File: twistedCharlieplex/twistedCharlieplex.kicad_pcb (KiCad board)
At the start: 2 copper layers, 54.9 x 54.9 mm, 69 parts

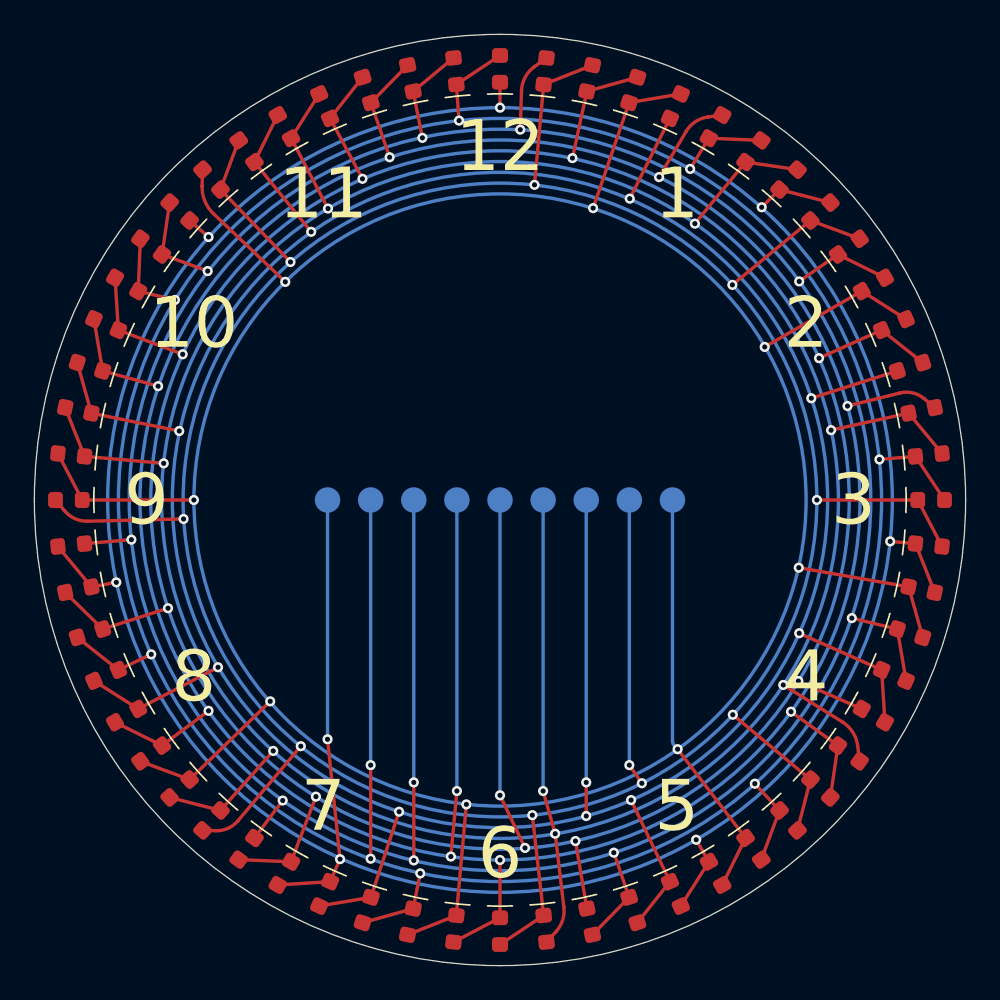
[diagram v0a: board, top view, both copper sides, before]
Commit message: Component layout locked. Trace nightmare time.
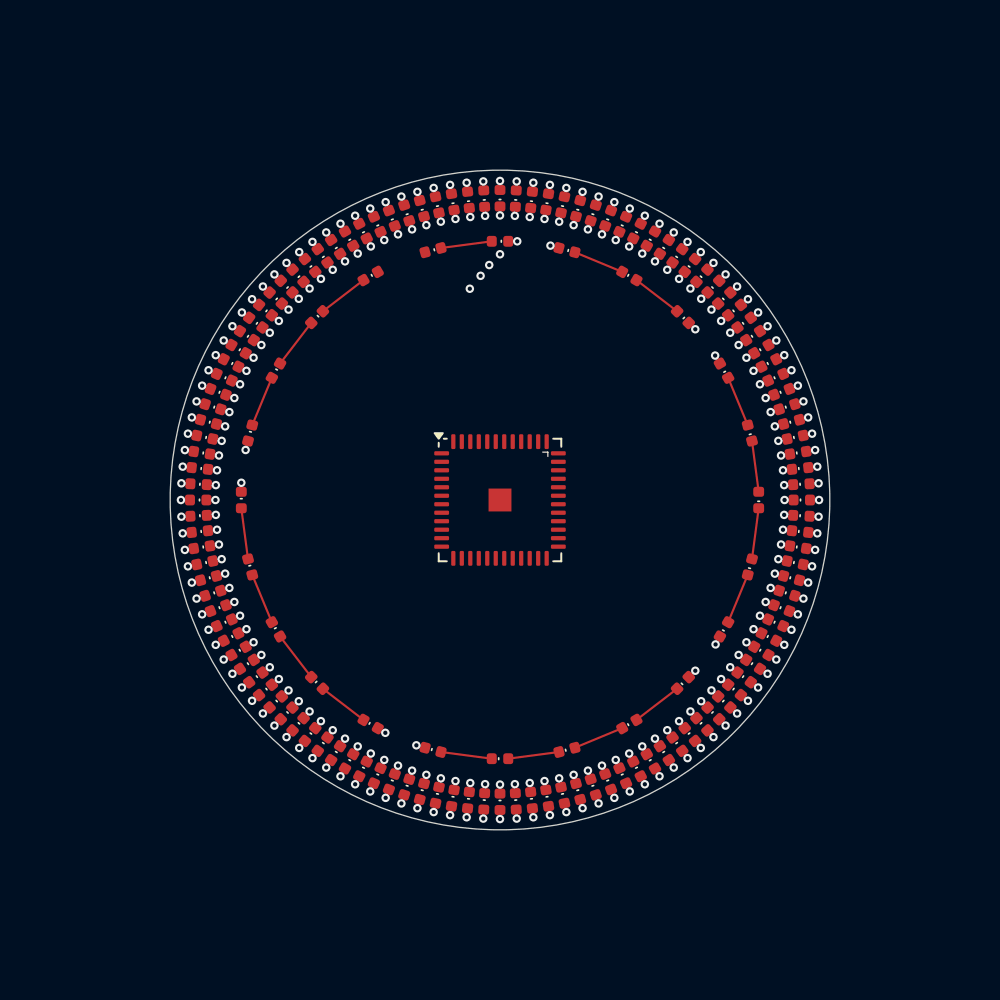
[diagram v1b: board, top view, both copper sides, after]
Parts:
- removed IO0, IO1, IO2, IO3, IO4, IO5, IO6, IO7, IO8: TestPoint, TestPoint:TestPoint_Pad_D1.5mm
- added D100: LED_Small, LED_SMD:LED_0402_1005Metric, F.Cu at (14.9, 9.68)
- added D101: LED_Small, LED_SMD:LED_0402_1005Metric, F.Cu at (15.8, 8.07)
- added D102: LED_Small, LED_SMD:LED_0402_1005Metric, F.Cu at (16.6, 6.37)
- added D103: LED_Small, LED_SMD:LED_0402_1005Metric, F.Cu at (17.2, 4.60)
- added D104: LED_Small, LED_SMD:LED_0402_1005Metric, F.Cu at (17.6, 2.78)
- added D105: LED_Small, LED_SMD:LED_0402_1005Metric, F.Cu at (17.8, 0.93)
- added D106: LED_Small, LED_SMD:LED_0402_1005Metric, F.Cu at (17.8, -0.93)
- added D107: LED_Small, LED_SMD:LED_0402_1005Metric, F.Cu at (17.6, -2.78)
- added D108: LED_Small, LED_SMD:LED_0402_1005Metric, F.Cu at (17.2, -4.60)
- added D109: LED_Small, LED_SMD:LED_0402_1005Metric, F.Cu at (16.6, -6.37)
- added D110: LED_Small, LED_SMD:LED_0402_1005Metric, F.Cu at (15.8, -8.07)
- added D111: LED_Small, LED_SMD:LED_0402_1005Metric, F.Cu at (14.9, -9.68)
- added D112: LED_Small, LED_SMD:LED_0402_1005Metric, F.Cu at (13.8, -11.2)
- added D113: LED_Small, LED_SMD:LED_0402_1005Metric, F.Cu at (12.6, -12.6)
- added D114: LED_Small, LED_SMD:LED_0402_1005Metric, F.Cu at (11.2, -13.8)
- added D115: LED_Small, LED_SMD:LED_0402_1005Metric, F.Cu at (9.68, -14.9)
- added D116: LED_Small, LED_SMD:LED_0402_1005Metric, F.Cu at (8.07, -15.8)
- added D117: LED_Small, LED_SMD:LED_0402_1005Metric, F.Cu at (6.37, -16.6)
- added D118: LED_Small, LED_SMD:LED_0402_1005Metric, F.Cu at (4.60, -17.2)
- added D119: LED_Small, LED_SMD:LED_0402_1005Metric, F.Cu at (2.78, -17.6)
- added D120: LED_Small, LED_SMD:LED_0402_1005Metric, F.Cu at (0.93, -17.8)
- added D121: LED_Small, LED_SMD:LED_0402_1005Metric, F.Cu at (-3.94, -14.7)
- added D122: LED_Small, LED_SMD:LED_0402_1005Metric, F.Cu at (-7.62, -13.2)
- added D123: LED_Small, LED_SMD:LED_0402_1005Metric, F.Cu at (-10.8, -10.8)
- added D124: LED_Small, LED_SMD:LED_0402_1005Metric, F.Cu at (-13.2, -7.62)
- added D125: LED_Small, LED_SMD:LED_0402_1005Metric, F.Cu at (-14.7, -3.94)
- added D126: LED_Small, LED_SMD:LED_0402_1005Metric, F.Cu at (-15.2, 0.00)
- added D127: LED_Small, LED_SMD:LED_0402_1005Metric, F.Cu at (-14.7, 3.94)
- added D128: LED_Small, LED_SMD:LED_0402_1005Metric, F.Cu at (-13.2, 7.62)
- added D129: LED_Small, LED_SMD:LED_0402_1005Metric, F.Cu at (-10.8, 10.8)
- added D130: LED_Small, LED_SMD:LED_0402_1005Metric, F.Cu at (-7.62, 13.2)
- added D131: LED_Small, LED_SMD:LED_0402_1005Metric, F.Cu at (-3.94, 14.7)
- added D132: LED_Small, LED_SMD:LED_0402_1005Metric, F.Cu at (0.00, 15.2)
- added D133: LED_Small, LED_SMD:LED_0402_1005Metric, F.Cu at (3.94, 14.7)
- added D134: LED_Small, LED_SMD:LED_0402_1005Metric, F.Cu at (7.62, 13.2)
- added D135: LED_Small, LED_SMD:LED_0402_1005Metric, F.Cu at (10.8, 10.8)
- added D136: LED_Small, LED_SMD:LED_0402_1005Metric, F.Cu at (13.2, 7.62)
- added D137: LED_Small, LED_SMD:LED_0402_1005Metric, F.Cu at (14.7, 3.94)
- added D138: LED_Small, LED_SMD:LED_0402_1005Metric, F.Cu at (15.2, 0.00)
- added D139: LED_Small, LED_SMD:LED_0402_1005Metric, F.Cu at (14.7, -3.94)
- added D140: LED_Small, LED_SMD:LED_0402_1005Metric, F.Cu at (13.2, -7.62)
- added D141: LED_Small, LED_SMD:LED_0402_1005Metric, F.Cu at (10.8, -10.8)
- added D142: LED_Small, LED_SMD:LED_0402_1005Metric, F.Cu at (7.62, -13.2)
- added D143: LED_Small, LED_SMD:LED_0402_1005Metric, F.Cu at (3.94, -14.7)
- added D144: LED_Small, LED_SMD:LED_0402_1005Metric, F.Cu at (0.00, -15.2)
- added D61: LED_Small, LED_SMD:LED_0402_1005Metric, F.Cu at (-0.93, -17.8)
- added D62: LED_Small, LED_SMD:LED_0402_1005Metric, F.Cu at (-2.78, -17.6)
- added D63: LED_Small, LED_SMD:LED_0402_1005Metric, F.Cu at (-4.60, -17.2)
- added D64: LED_Small, LED_SMD:LED_0402_1005Metric, F.Cu at (-6.37, -16.6)
- added D65: LED_Small, LED_SMD:LED_0402_1005Metric, F.Cu at (-8.07, -15.8)
- added D66: LED_Small, LED_SMD:LED_0402_1005Metric, F.Cu at (-9.68, -14.9)
- added D67: LED_Small, LED_SMD:LED_0402_1005Metric, F.Cu at (-11.2, -13.8)
- added D68: LED_Small, LED_SMD:LED_0402_1005Metric, F.Cu at (-12.6, -12.6)
- added D69: LED_Small, LED_SMD:LED_0402_1005Metric, F.Cu at (-13.8, -11.2)
- added D70: LED_Small, LED_SMD:LED_0402_1005Metric, F.Cu at (-14.9, -9.68)
- added D71: LED_Small, LED_SMD:LED_0402_1005Metric, F.Cu at (-15.8, -8.07)
- added D72: LED_Small, LED_SMD:LED_0402_1005Metric, F.Cu at (-16.6, -6.37)
- added D73: LED_Small, LED_SMD:LED_0402_1005Metric, F.Cu at (-17.2, -4.60)
- added D74: LED_Small, LED_SMD:LED_0402_1005Metric, F.Cu at (-17.6, -2.78)
- added D75: LED_Small, LED_SMD:LED_0402_1005Metric, F.Cu at (-17.8, -0.93)
- added D76: LED_Small, LED_SMD:LED_0402_1005Metric, F.Cu at (-17.8, 0.93)
- added D77: LED_Small, LED_SMD:LED_0402_1005Metric, F.Cu at (-17.6, 2.78)
- added D78: LED_Small, LED_SMD:LED_0402_1005Metric, F.Cu at (-17.2, 4.60)
- added D79: LED_Small, LED_SMD:LED_0402_1005Metric, F.Cu at (-16.6, 6.37)
- added D80: LED_Small, LED_SMD:LED_0402_1005Metric, F.Cu at (-15.8, 8.07)
- added D81: LED_Small, LED_SMD:LED_0402_1005Metric, F.Cu at (-14.9, 9.68)
- added D82: LED_Small, LED_SMD:LED_0402_1005Metric, F.Cu at (-13.8, 11.2)
- added D83: LED_Small, LED_SMD:LED_0402_1005Metric, F.Cu at (-12.6, 12.6)
- added D84: LED_Small, LED_SMD:LED_0402_1005Metric, F.Cu at (-11.2, 13.8)
- added D85: LED_Small, LED_SMD:LED_0402_1005Metric, F.Cu at (-9.68, 14.9)
- added D86: LED_Small, LED_SMD:LED_0402_1005Metric, F.Cu at (-8.07, 15.8)
- added D87: LED_Small, LED_SMD:LED_0402_1005Metric, F.Cu at (-6.37, 16.6)
- added D88: LED_Small, LED_SMD:LED_0402_1005Metric, F.Cu at (-4.60, 17.2)
- added D89: LED_Small, LED_SMD:LED_0402_1005Metric, F.Cu at (-2.78, 17.6)
- added D90: LED_Small, LED_SMD:LED_0402_1005Metric, F.Cu at (-0.93, 17.8)
- added D91: LED_Small, LED_SMD:LED_0402_1005Metric, F.Cu at (0.93, 17.8)
- added D92: LED_Small, LED_SMD:LED_0402_1005Metric, F.Cu at (2.78, 17.6)
- added D93: LED_Small, LED_SMD:LED_0402_1005Metric, F.Cu at (4.60, 17.2)
- added D94: LED_Small, LED_SMD:LED_0402_1005Metric, F.Cu at (6.37, 16.6)
- added D95: LED_Small, LED_SMD:LED_0402_1005Metric, F.Cu at (8.07, 15.8)
- added D96: LED_Small, LED_SMD:LED_0402_1005Metric, F.Cu at (9.68, 14.9)
- added D97: LED_Small, LED_SMD:LED_0402_1005Metric, F.Cu at (11.2, 13.8)
- added D98: LED_Small, LED_SMD:LED_0402_1005Metric, F.Cu at (12.6, 12.6)
- added D99: LED_Small, LED_SMD:LED_0402_1005Metric, F.Cu at (13.8, 11.2)
- added U2: STM32L412CBUxP, Package_DFN_QFN:QFN-48-1EP_7x7mm_P0.5mm_EP5.6x5.6mm, F.Cu at (0.00, 0.00)
- D1, D10, D11, D12, D13, D14, D15, D16, D17, D18, D19, D2, D20, D21, D22, D23, D24, D25, D26, D27, D28, D29, D3, D30, D31, D32, D33, D34, D35, D36, D37, D38, D39, D4, D40, D41, D42, D43, D44, D45, D46, D47, D48, D49, D5, D50, D51, D52, D53, D54, D55, D56, D57, D58, D59, D6, D60, D7, D8, D9: footprint LED_SMD:LED_0603_1608Metric -> LED_SMD:LED_0402_1005Metric
- moved D13 7.62 mm to (-16.9, -5.49)
- moved D19 7.62 mm to (-16.9, 5.49)
- moved D28 7.62 mm to (-5.49, 16.9)
- moved D34 7.62 mm to (5.49, 16.9)
- moved D4 7.62 mm to (-5.49, -16.9)
- moved D43 7.62 mm to (16.9, 5.49)
- moved D49 7.62 mm to (16.9, -5.49)
- moved D58 7.62 mm to (5.49, -16.9)
- moved D12 7.62 mm to (-16.2, -7.23)
- moved D20 7.62 mm to (-16.2, 7.23)
- moved D27 7.62 mm to (-7.23, 16.2)
- moved D35 7.62 mm to (7.23, 16.2)
- moved D42 7.62 mm to (16.2, 7.23)
- moved D5 7.62 mm to (-7.23, -16.2)
- moved D50 7.62 mm to (16.2, -7.23)
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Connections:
- net /IO0 renamed /Charlie Displays/IO0
- net /IO1 renamed /Charlie Displays/IO1
- net /IO2 renamed /Charlie Displays/IO2
- net /IO3 renamed /Charlie Displays/IO3
- net /IO4 renamed /Charlie Displays/IO4
- net /IO5 renamed /Charlie Displays/IO5
- net /IO6 renamed /Charlie Displays/IO6
- net /IO7 renamed /Charlie Displays/IO7
- net /IO8 renamed /Charlie Displays/IO8
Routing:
- net /Charlie Displays/IO8: track 91.1 -> 27.2 mm, vias 8 -> 15
- net /Charlie Displays/IO7: track 87.1 -> 24.0 mm, vias 10 -> 14
- net /Charlie Displays/IO6: track 79.6 -> 24.0 mm, vias 10 -> 14
- net /Charlie Displays/IO5: track 72.1 -> 20.1 mm, vias 8 -> 12
- net /Charlie Displays/IO4: track 71.8 -> 24.0 mm, vias 10 -> 14
- net /Charlie Displays/IO3: track 64.6 -> 20.1 mm, vias 9 -> 12
- net /Charlie Displays/IO2: track 61.0 -> 20.7 mm, vias 10 -> 13
- net /Charlie Displays/IO11: track 0.00 -> 30.9 mm, vias 0 -> 15
- net /Charlie Displays/IO1: track 57.8 -> 30.2 mm, vias 9 -> 15
- net /Charlie Displays/IO18: track 0.00 -> 27.2 mm, vias 0 -> 15
- net /Charlie Displays/IO16: track 0.00 -> 24.0 mm, vias 0 -> 14
- net /Charlie Displays/IO17: track 0.00 -> 24.0 mm, vias 0 -> 14
- net /Charlie Displays/IO14: track 0.00 -> 24.0 mm, vias 0 -> 14
- net /Charlie Displays/IO10: track 0.00 -> 23.0 mm, vias 0 -> 13
- net /Charlie Displays/IO12: track 0.00 -> 20.7 mm, vias 0 -> 13
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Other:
- board size 54.9 x 54.9 mm -> 38.9 x 38.9 mm
- copper layers 2 -> 6
- board text removed: "1"
- board text removed: "10"
- board text removed: "11"
- board text removed: "12"
- board text removed: "2"
- board text removed: "3"
- board text removed: "4"
- board text removed: "5"
- board text removed: "6"
- board text removed: "7"
- board text removed: "8"
- board text removed: "9"

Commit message: Start of a layout. This is awful. I'm not sure I can make this happen in 4 layers. I may come back to this.
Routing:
- net /Charlie Displays/IO2: track 20.7 -> 48.9 mm, vias 13 -> 16
- net /Charlie Displays/IO12: track 20.7 -> 47.2 mm, vias 13 -> 16
- net /Charlie Displays/IO8: track 27.2 -> 49.1 mm, vias 15 -> 18
- net /Charlie Displays/IO1: track 30.2 -> 51.5 mm, vias 15 -> 16
- net /Charlie Displays/IO11: track 30.9 -> 48.0 mm, vias 15 -> 16
- net /Charlie Displays/IO18: track 27.2 -> 44.1 mm, vias 15 -> 18
- net /Charlie Displays/IO7: track 24.0 -> 38.4 mm, vias 14 -> 16
- net /Charlie Displays/IO6: track 24.0 -> 37.6 mm, vias 14 -> 15
- net /Charlie Displays/IO16: track 24.0 -> 36.6 mm, vias 14 -> 15
- net /Charlie Displays/IO17: track 24.0 -> 36.2 mm, vias 14 -> 16
- net /Charlie Displays/IO4: track 24.0 -> 33.8 mm, vias 14 -> 15
- net /Charlie Displays/IO13: track 20.1 -> 29.8 mm, vias 12 -> 13
- net /Charlie Displays/IO15: track 20.1 -> 29.6 mm, vias 12 -> 14
- net /Charlie Displays/IO14: track 24.0 -> 33.0 mm, vias 14 -> 15
- net /Charlie Displays/IO5: track 20.1 -> 28.5 mm, vias 12 -> 14
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
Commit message: spirograph layout. let the nightmares begin
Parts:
- added AE1: Antenna_Shield, Antenna_SMD:C209892, F.Cu at (8.99, -3.30)
- added C1: 100n, Capacitor_SMD:C_0402_1005Metric, F.Cu at (-1.75, -7.47)
- added C2: 10u, Capacitor_SMD:C_0402_1005Metric, F.Cu at (-2.69, -7.47)
- added C3: 100n, Capacitor_SMD:C_0402_1005Metric, F.Cu at (-4.62, 0.51)
- added C4: 4p3, Capacitor_SMD:C_0402_1005Metric, F.Cu at (-7.90, -2.44)
- added C5: 4p3, Capacitor_SMD:C_0402_1005Metric, F.Cu at (-7.90, -0.61)
- added C6: 12p, Capacitor_SMD:C_0402_1005Metric, F.Cu at (11.2, 1.17)
- added C7: 12p, Capacitor_SMD:C_0402_1005Metric, F.Cu at (11.2, -1.93)
- added Q1: Q_PMOS_GSD, Package_TO_SOT_SMD:SOT-523, F.Cu at (25.7, -4.34)
- added R1: 10k, Resistor_SMD:R_0402_1005Metric, F.Cu at (-1.50, -4.62)
- added R2: 10k, Resistor_SMD:R_0402_1005Metric, F.Cu at (0.79, -4.65)
- added R3: 10k, Resistor_SMD:R_0402_1005Metric, F.Cu at (0.25, -5.61)
- added R4: 100k, Resistor_SMD:R_0402_1005Metric, F.Cu at (5.49, -3.58)
- added R5: 1M, Resistor_SMD:R_0402_1005Metric, F.Cu at (24.1, -4.34)
- added U1: STM32L412CBUx, Package_DFN_QFN:QFN-48-1EP_7x7mm_P0.5mm_EP5.6x5.6mm, F.Cu at (0.00, 0.00)
- added U3: ESP32-C3, Package_DFN_QFN:QFN-32-1EP_5x5mm_P0.5mm_EP3.7x3.7mm, F.Cu at (7.24, 0.00)
- added Y1: 32.768k, Crystal:Crystal_SMD_3215-2Pin_3.2x1.5mm, F.Cu at (-6.27, -1.52)
- added Y2: 40M, SMD_Crystal:Crystal_SMD_1612_4P, F.Cu at (11.2, -0.25)
- U2: value STM32L412CBUxP -> LIS2DW12; footprint Package_DFN_QFN:QFN-48-1EP_7x7mm_P0.5mm_EP5.6x5.6mm -> Package_LGA:LGA-12_2x2mm_P0.5mm
- moved U2 7.47 mm to (0.00, -7.47), turned to 180 degrees
- moved D122 4.19 mm to (-4.17, -15.6), turned to -165 degrees
- moved D128 4.19 mm to (-15.6, 4.17), turned to -75 degrees
- moved D134 4.19 mm to (4.17, 15.6), turned to 15 degrees
- moved D140 4.19 mm to (15.6, -4.17), turned to 105 degrees
- moved D121 4.19 mm to (0.00, -16.1), turned to 180 degrees
- moved D127 4.19 mm to (-16.1, 0.00), turned to -90 degrees
- moved D133 4.19 mm to (0.00, 16.1), turned to 0 degrees
- moved D139 4.19 mm to (16.1, 0.00), turned to 90 degrees
- moved D123 4.19 mm to (-8.06, -14.0), turned to -150 degrees
- moved D129 4.19 mm to (-14.0, 8.06), turned to -60 degrees
- moved D135 4.19 mm to (8.06, 14.0), turned to 30 degrees
- moved D141 4.19 mm to (14.0, -8.06), turned to 120 degrees
- moved D125 4.19 mm to (-14.0, -8.06), turned to -120 degrees
- moved D131 4.19 mm to (-8.06, 14.0), turned to -30 degrees
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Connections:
- net /Charlie Displays/IO0 renamed IO0
- net /Charlie Displays/IO1 renamed IO1
- net /Charlie Displays/IO10 renamed IO10
- net /Charlie Displays/IO11 renamed IO11
- net /Charlie Displays/IO12 renamed IO12
- net /Charlie Displays/IO13 renamed IO13
- net /Charlie Displays/IO14 renamed IO14
- net /Charlie Displays/IO15 renamed IO15
- net /Charlie Displays/IO16 renamed IO16
- net /Charlie Displays/IO17 renamed IO17
- net /Charlie Displays/IO18 renamed IO18
- net /Charlie Displays/IO2 renamed IO2
- net /Charlie Displays/IO20 renamed IO20
- net /Charlie Displays/IO21 renamed IO21
- net /Charlie Displays/IO22 renamed IO22
- net /Charlie Displays/IO23 renamed IO23
- net /Charlie Displays/IO24 renamed IO24
- net /Charlie Displays/IO25 renamed IO25
- net /Charlie Displays/IO3 renamed IO3
- net /Charlie Displays/IO4 renamed IO4
- net /Charlie Displays/IO5 renamed IO5
- net /Charlie Displays/IO6 renamed IO6
- net /Charlie Displays/IO7 renamed IO7
- net /Charlie Displays/IO8 renamed IO8
- U2 pad 1: VCC -> SCL
- U2 pad 10: unconnected-(U2-PA0-Pad10) -> +3V0
- U2 pad 12: unconnected-(U2-PA2-Pad12) -> WKUP1
- U2 pad 4: unconnected-(U2-PC15-Pad4) -> SDA
- U2 pad 6: unconnected-(U2-PH1-Pad6) -> GND
- U2 pad 7: unconnected-(U2-NRST-Pad7) -> GND
- U2 pad 9: VCC -> +3V0
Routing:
- net IO14: track 33.0 -> 146.0 mm, vias 15 -> 17
- net IO6: track 37.6 -> 146.9 mm, vias 15 -> 16
- net IO3: track 23.7 -> 130.1 mm, vias 12 -> 13
- net IO15: track 29.6 -> 131.3 mm, vias 14 -> 13
- net IO4: track 33.8 -> 135.5 mm, vias 15 -> 16
- net IO5: track 28.5 -> 129.0 mm, vias 14 -> 13
- net IO10: track 20.7 -> 121.0 mm, vias 13 -> 14
- net IO0: track 38.8 -> 138.2 mm, vias 15 -> 14
- net IO13: track 29.8 -> 119.7 mm, vias 13 -> 12
- net IO16: track 36.6 -> 126.3 mm, vias 15 -> 16
- net IO17: track 36.2 -> 122.9 mm, vias 16 -> 15
- net IO7: track 38.4 -> 124.7 mm, vias 16 -> 14
- net IO1: track 51.5 -> 136.4 mm, vias 16 -> 14
- net IO2: track 48.9 -> 130.0 mm, vias 16 -> 15
- net IO18: track 44.1 -> 123.9 mm, vias 18 -> 15
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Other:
- copper layers 6 -> 4

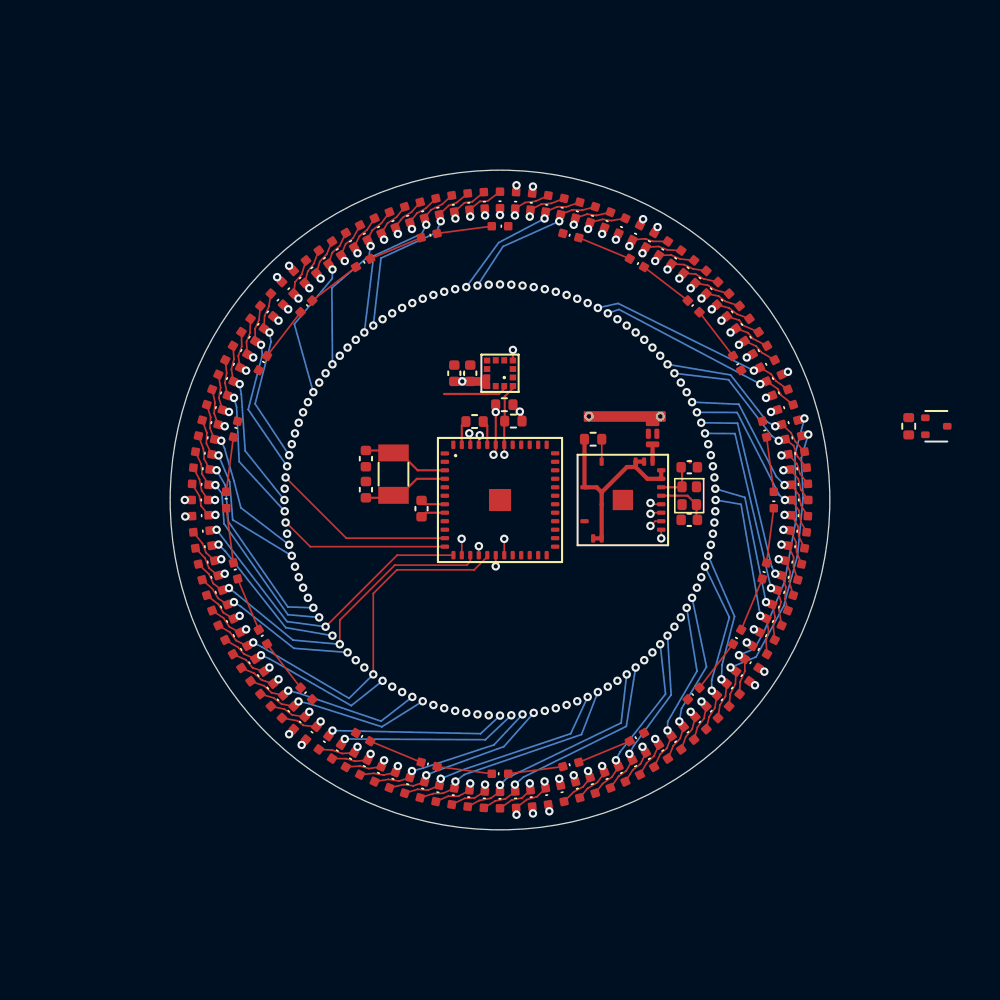
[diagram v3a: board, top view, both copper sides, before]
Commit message: Layout is solving. It's not pretty, but it's theoretically electrically sound.
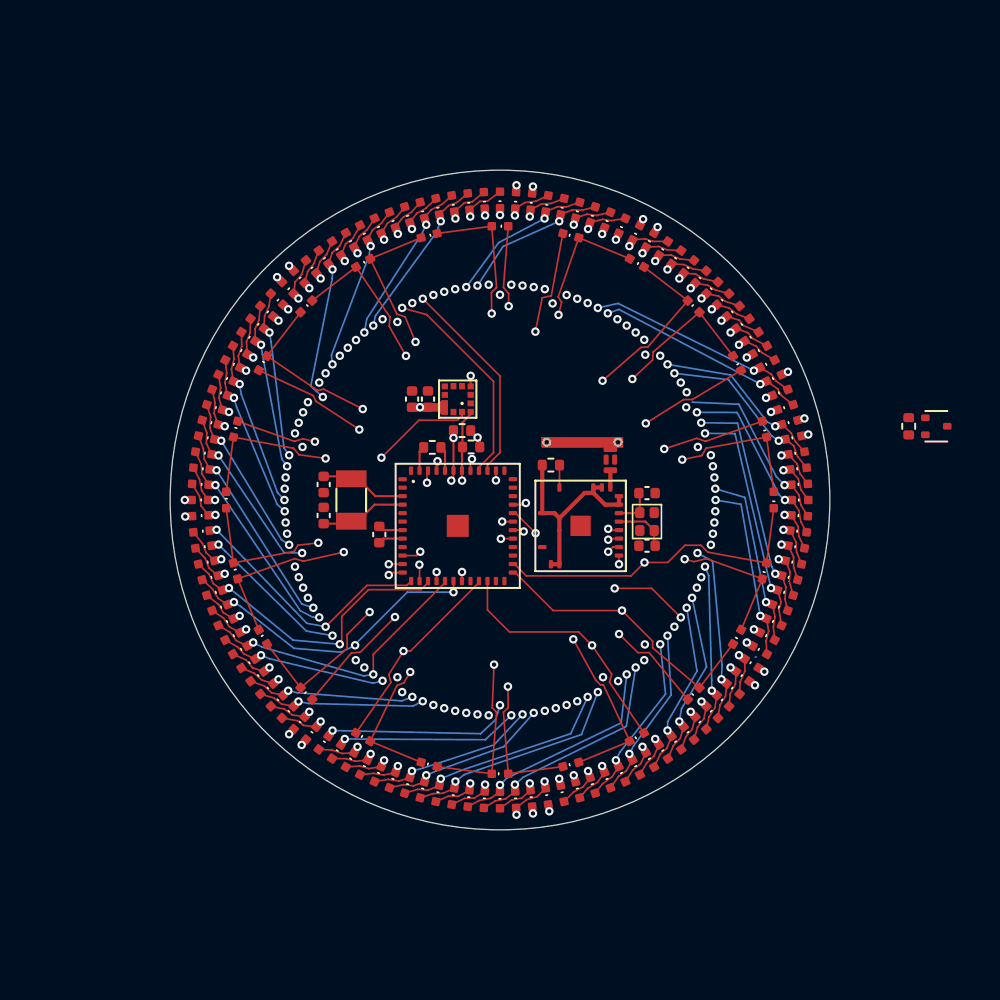
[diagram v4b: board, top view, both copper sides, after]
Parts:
- moved AE1 2.92 mm to (6.50, -1.78)
- moved C2 2.92 mm to (-5.18, -5.94)
- moved C3 2.92 mm to (-7.11, 2.03)
- moved C4 2.92 mm to (-10.4, -0.91)
- moved C5 2.92 mm to (-10.4, 0.91)
- moved C6 2.92 mm to (8.66, 2.69)
- moved C7 2.92 mm to (8.66, -0.41)
- moved R1 2.92 mm to (-3.99, -3.10)
- moved R2 2.92 mm to (-1.70, -3.12)
- moved R3 2.92 mm to (-2.24, -4.09)
- moved R4 2.92 mm to (3.00, -2.06)
- moved U1 2.92 mm to (-2.49, 1.52)
- moved U2 2.92 mm to (-2.49, -5.94)
- moved U3 2.92 mm to (4.75, 1.52)
- moved Y1 2.92 mm to (-8.76, 0.00)
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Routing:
- net IO25: track 9.75 -> 53.9 mm, vias 0 -> 5
- net IO24: track 13.0 -> 53.1 mm, vias 0 -> 5
- net IO23: track 6.50 -> 46.2 mm, vias 0 -> 5
- net IO22: track 9.75 -> 44.6 mm, vias 0 -> 5
- net IO20: track 10.3 -> 42.4 mm, vias 1 -> 6
- net IO21: track 13.7 -> 43.7 mm, vias 1 -> 5
- net IO17: track 122.9 -> 136.7 mm
- net IO11: track 126.9 -> 140.4 mm, vias 14 -> 15
- net IO18: track 123.9 -> 136.4 mm, vias 15 -> 16
- net IO7: track 124.7 -> 136.5 mm, vias 14 -> 15
- net IO16: track 126.3 -> 138.0 mm
- net IO13: track 119.7 -> 131.4 mm, vias 12 -> 13
- net IO10: track 121.0 -> 132.3 mm, vias 14 -> 15
- net IO8: track 124.6 -> 135.5 mm, vias 16 -> 17
- net WKUP1: track 3.83 -> 14.6 mm, vias 0 -> 2
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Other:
- board text added: "ring of fireeee"
